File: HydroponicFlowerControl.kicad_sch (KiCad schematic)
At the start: 4 parts

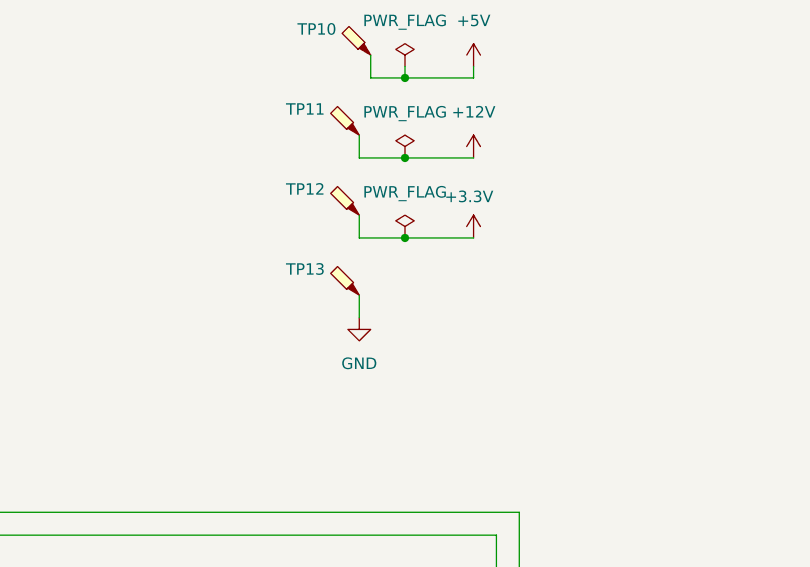
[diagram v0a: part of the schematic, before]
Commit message: Fix ERC warnings
See #28
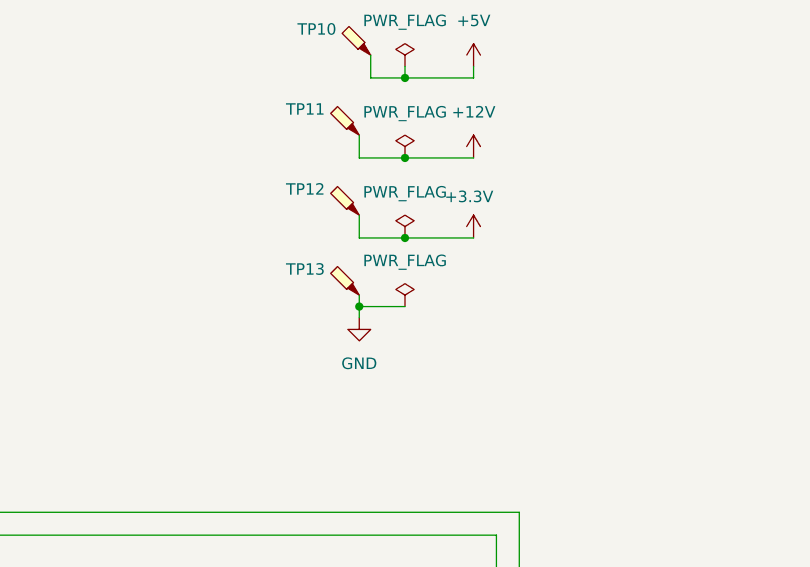
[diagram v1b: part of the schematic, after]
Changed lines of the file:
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@@
+	)
+	(junction
+		(at 104.14 49.53)
+		(diameter 0)
+		(color 0 0 0 0)
 	)
 	(junction
@@
 	(wire
 		(pts
+			(xy 104.14 49.53) (xy 104.14 50.8)
+		)
+		(stroke
+			(width 0)
+			(type default)
+		)
+	)
+	(wire
+		(pts
 			(xy 104.14 39.37) (xy 104.14 41.91)
 		)
@@
 	(wire
 		(pts
-			(xy 104.14 48.26) (xy 104.14 50.8)
+			(xy 104.14 48.26) (xy 104.14 49.53)
 		)
 		(stroke
@@
 		(pts
 			(xy 104.14 33.02) (xy 109.22 33.02)
+		)
+		(stroke
+			(width 0)
+			(type default)
+		)
+	)
+	(wire
+		(pts
+			(xy 104.14 49.53) (xy 109.22 49.53)
 		)
 		(stroke
@@
 	(symbol
 		(lib_id "power:PWR_FLAG")
+		(at 109.22 49.53 0)
+		(unit 1)
+		(exclude_from_sim no)
+		(in_bom yes)
+		(on_board yes)
+		(dnp no)
+		(fields_autoplaced yes)
+		(property "Reference" "#FLG04"
+			(at 109.22 47.625 0)
+			(effects
+				(font
+					(size 1.27 1.27)
+				)
+				(hide yes)
+			)
+		)
+		(property "Value" "PWR_FLAG"
+			(at 109.22 44.45 0)
+			(effects
+				(font
+					(size 1.27 1.27)
+				)
+			)
+		)
+		(property "Footprint" ""
+			(at 109.22 49.53 0)
+			(effects
+				(font
+					(size 1.27 1.27)
+				)
+				(hide yes)
+			)
+		)
+		(property "Datasheet" "~"
+			(at 109.22 49.53 0)
+			(effects
+				(font
+					(size 1.27 1.27)
+				)
+				(hide yes)
+			)
+		)
+		(property "Description" "Special symbol for telling ERC where power comes from"
+			(at 109.22 49.53 0)
+			(effects
+				(font
+					(size 1.27 1.27)
+				)
+				(hide yes)
+			)
+		)
+		(pin "1"
+		)
+		(instances
+			(project "HydroponicFlowerControl"
+				(path "/b3c8a28b-9ce1-4002-b8e8-ef8cb73fe031"
+					(reference "#FLG04")
+					(unit 1)
+				)
+			)
+		)
+	)
+	(symbol
+		(lib_name "PWR_FLAG_1")
+		(lib_id "power:PWR_FLAG")
 		(at 109.22 41.91 0)

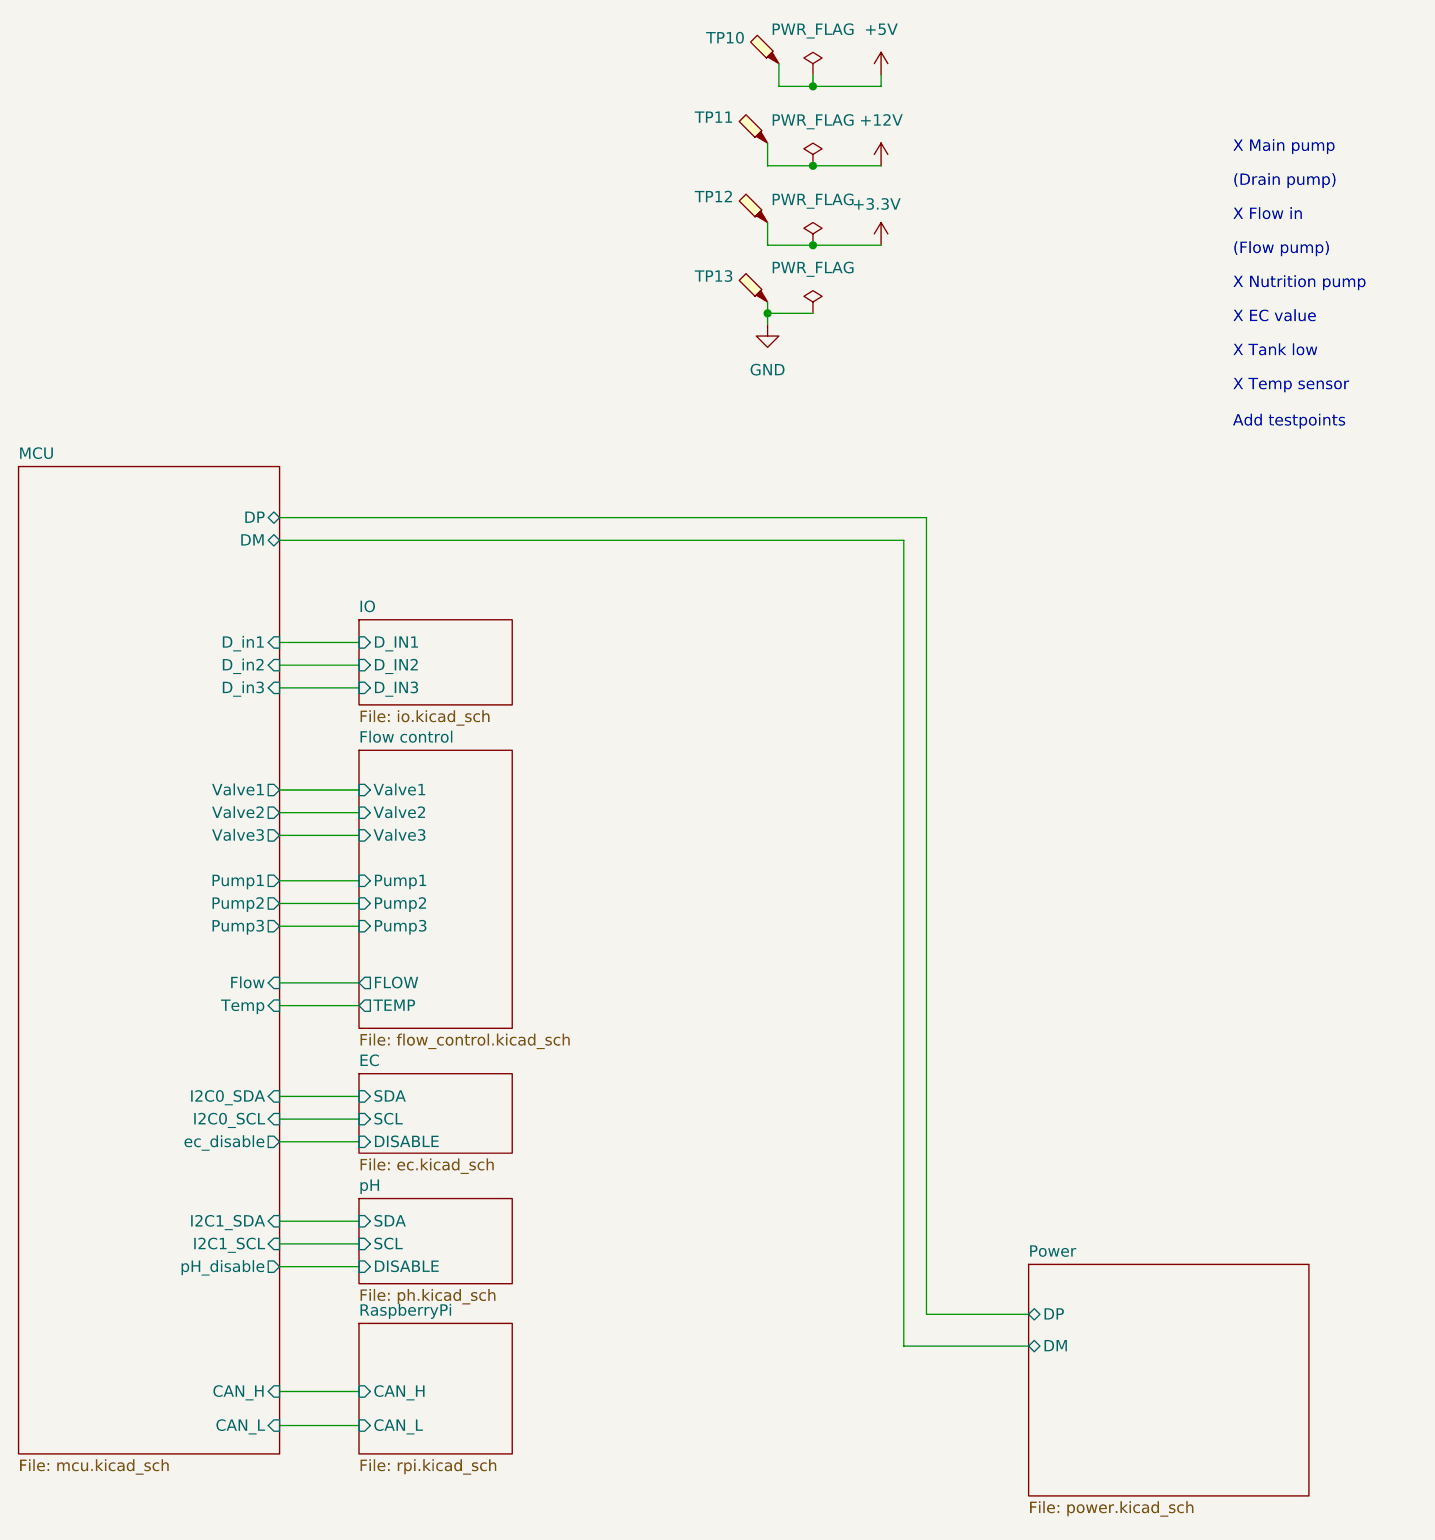
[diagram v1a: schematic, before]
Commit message: Fix ERC errors
Closes #28
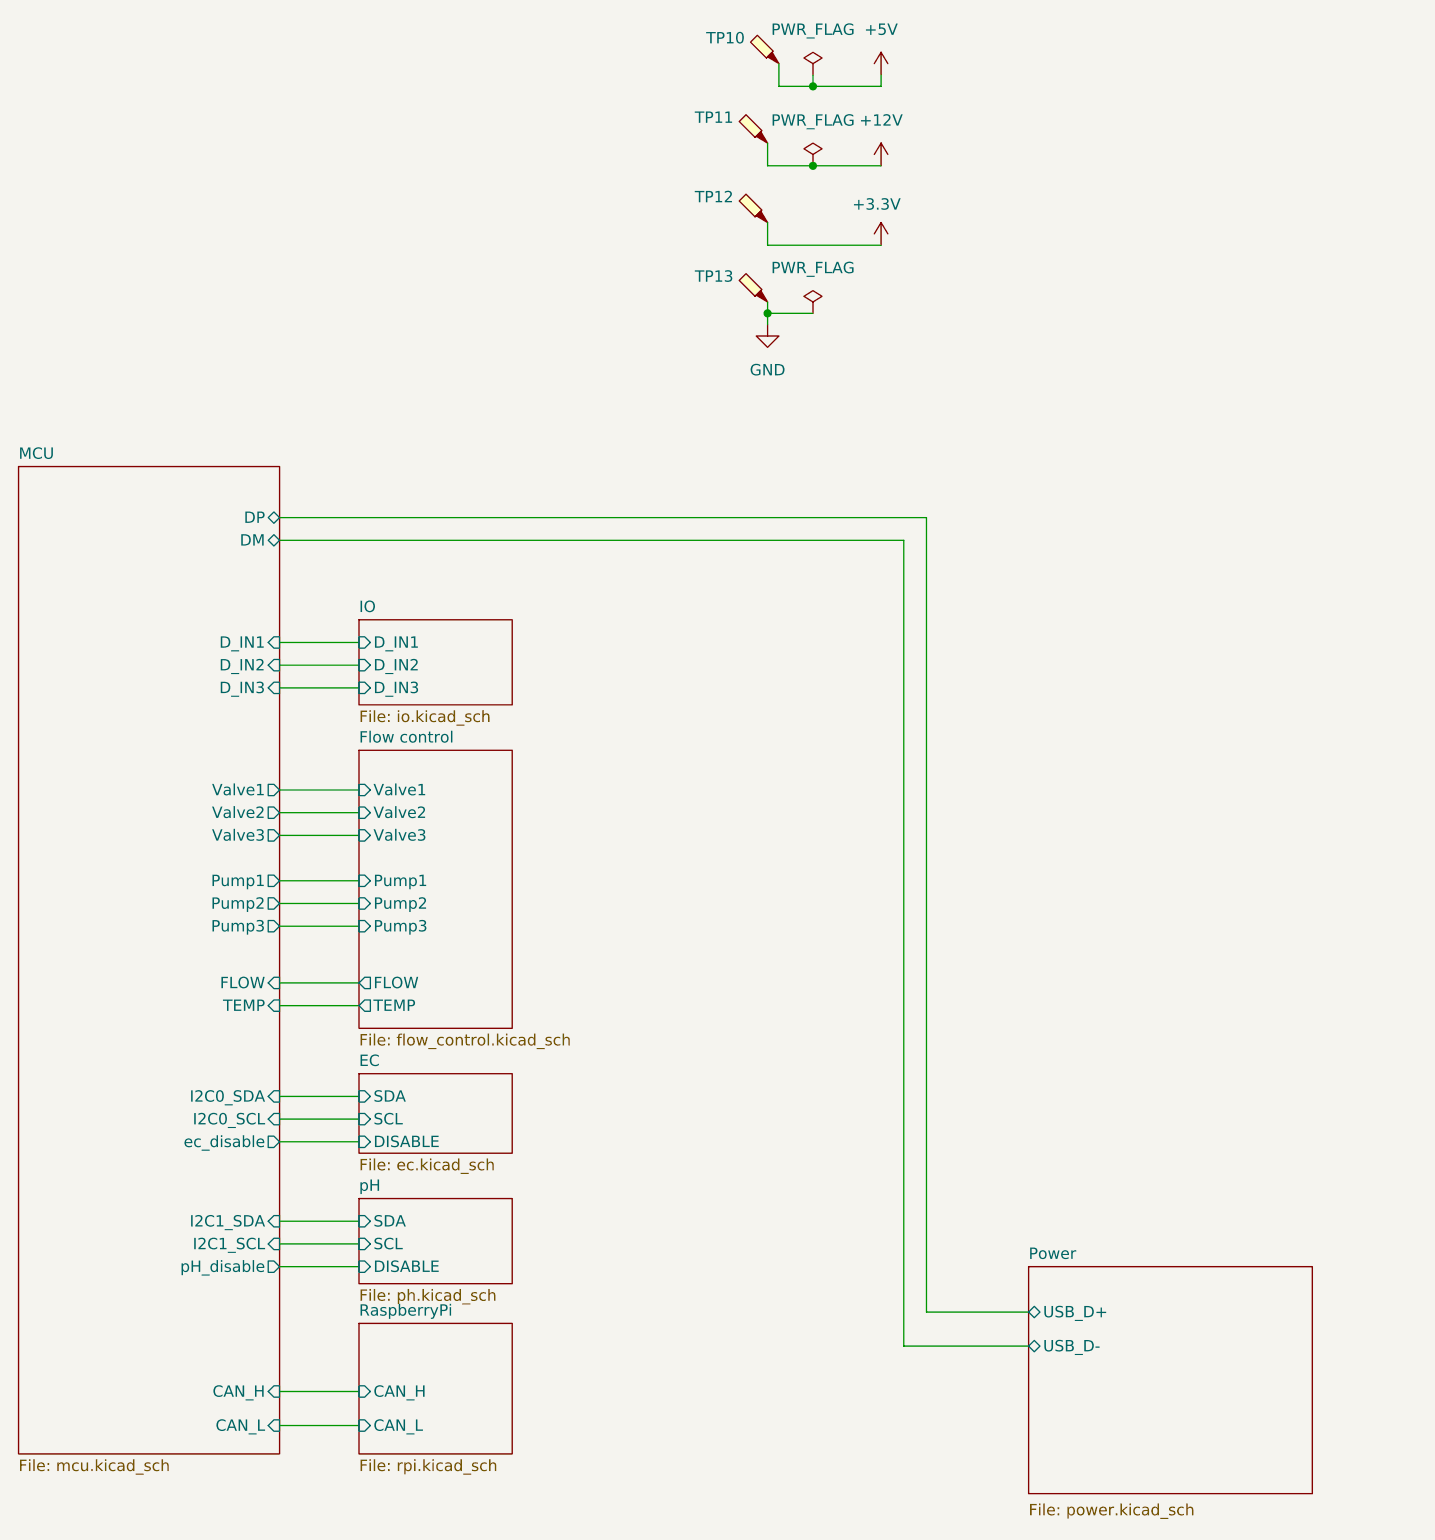
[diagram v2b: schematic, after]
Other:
- sheet MCU ports: added D_IN1, D_IN2, D_IN3, FLOW, TEMP; removed D_in1, D_in2, D_in3, Flow, Temp
- sheet Power ports: added USB_D+, USB_D-; removed DM, DP
- note removed: "(Drain pump)"
- note removed: "(Flow pump)"
- note removed: "Add testpoints"
- note removed: "X EC value"
- note removed: "X Flow in"
- note removed: "X Main pump"
- note removed: "X Nutrition pump"
- note removed: "X Tank low"
- note removed: "X Temp sensor"
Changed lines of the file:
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@@
-	)
-	(junction
-		(at 109.22 41.91)
-		(diameter 0)
-		(color 0 0 0 0)
 	)
 	(junction
@@
 	(wire
 		(pts
-			(xy 121.92 72.39) (xy 121.92 161.544)
+			(xy 121.92 72.39) (xy 121.92 161.29)
 		)
 		(stroke
@@
 	(wire
 		(pts
-			(xy 109.22 41.91) (xy 116.84 41.91)
-		)
-		(stroke
-			(width 0)
-			(type default)
-		)
-	)
-	(wire
-		(pts
 			(xy 49.53 153.67) (xy 58.42 153.67)
 		)
@@
 	(wire
 		(pts
-			(xy 121.92 161.544) (xy 133.35 161.544)
+			(xy 121.92 161.29) (xy 133.35 161.29)
 		)
 		(stroke
@@
 	(wire
 		(pts
-			(xy 104.14 41.91) (xy 109.22 41.91)
+			(xy 104.14 41.91) (xy 116.84 41.91)
 		)
 		(stroke
@@
 			(width 0)
 			(type default)
-		)
-	)
-	(text "X Tank low"
-		(exclude_from_sim no)
-		(at 156.21 54.61 0)
-		(effects
-			(font
-				(size 1.27 1.27)
-			)
-			(justify left bottom)
-		)
-	)
-	(text "X Temp sensor"
-		(exclude_from_sim no)
-		(at 156.21 58.42 0)
-		(effects
-			(font
-				(size 1.27 1.27)
-			)
-			(justify left bottom)
-		)
-	)
-	(text "X EC value"
-		(exclude_from_sim no)
-		(at 156.21 50.8 0)
-		(effects
-			(font
-				(size 1.27 1.27)
-			)
-			(justify left bottom)
-		)
-	)
-	(text "(Drain pump)"
-		(exclude_from_sim no)
-		(at 156.21 35.56 0)
-		(effects
-			(font
-				(size 1.27 1.27)
-			)
-			(justify left bottom)
-		)
-	)
-	(text "(Flow pump)"
-		(exclude_from_sim no)
-		(at 156.21 43.18 0)
-		(effects
-			(font
-				(size 1.27 1.27)
-			)
-			(justify left bottom)
-		)
-	)
-	(text "X Flow in"
-		(exclude_from_sim no)
-		(at 156.21 39.37 0)
-		(effects
-			(font
-				(size 1.27 1.27)
-			)
-			(justify left bottom)
-		)
-	)
-	(text "X Main pump"
-		(exclude_from_sim no)
-		(at 156.21 31.75 0)
-		(effects
-			(font
-				(size 1.27 1.27)
-			)
-			(justify left bottom)
-		)
-	)
-	(text "Add testpoints"
-		(exclude_from_sim no)
-		(at 156.21 62.484 0)
-		(effects
-			(font
-				(size 1.27 1.27)
-			)
-			(justify left bottom)
-		)
-	)
-	(text "X Nutrition pump"
-		(exclude_from_sim no)
-		(at 156.21 46.99 0)
-		(effects
-			(font
-				(size 1.27 1.27)
-			)
-			(justify left bottom)
 		)
 	)
@@
 	)
 	(symbol
-		(lib_name "PWR_FLAG_1")
-		(lib_id "power:PWR_FLAG")
-		(at 109.22 41.91 0)
-		(unit 1)
-		(exclude_from_sim no)
-		(in_bom yes)
-		(on_board yes)
-		(dnp no)
-		(fields_autoplaced yes)
-		(property "Reference" "#FLG03"
-			(at 109.22 40.005 0)
-			(effects
-				(font
-					(size 1.27 1.27)
-				)
-				(hide yes)
-			)
-		)
-		(property "Value" "PWR_FLAG"
-			(at 109.22 36.83 0)
-			(effects
-				(font
-					(size 1.27 1.27)
-				)
-			)
-		)
-		(property "Footprint" ""
-			(at 109.22 41.91 0)
-			(effects
-				(font
-					(size 1.27 1.27)
-				)
-				(hide yes)
-			)
-		)
-		(property "Datasheet" "~"
-			(at 109.22 41.91 0)
-			(effects
-				(font
-					(size 1.27 1.27)
-				)
-				(hide yes)
-			)
-		)
-		(property "Description" "Special symbol for telling ERC where power comes from"
-			(at 109.22 41.91 0)
-			(effects
-				(font
-					(size 1.27 1.27)
-				)
-				(hide yes)
-			)
-		)
-		(pin "1"
-		)
-		(instances
-			(project "HydroponicFlowerControl"
-				(path "/b3c8a28b-9ce1-4002-b8e8-ef8cb73fe031"
-					(reference "#FLG03")
-					(unit 1)
-				)
-			)
-		)
-	)
-	(symbol
 		(lib_id "power:+3.3V")
 		(at 116.84 41.91 0)
@@
 	)
 	(sheet
-		(at 133.35 155.956)
-		(size 31.369 25.908)
+		(at 133.35 156.21)
+		(size 31.75 25.4)
 		(fields_autoplaced yes)
 		(stroke
@@
 		)
 		(property "Sheetname" "Power"
-			(at 133.35 155.2444 0)
+			(at 133.35 155.4984 0)
 			(effects
 				(font
@@
 		)
 		(property "Sheetfile" "power.kicad_sch"
-			(at 133.35 182.4486 0)
+			(at 133.35 182.7026 0)
 			(effects
 				(font
@@
 			)
 		)
-		(pin "DP" bidirectional
-			(at 133.35 161.544 180)
-			(effects
-				(font
-					(size 1.27 1.27)
-				)
-				(justify left)
-			)
-		)
-		(pin "DM" bidirectional
+		(pin "USB_D-" bidirectional
 			(at 133.35 165.1 180)
+			(effects
+				(font
+					(size 1.27 1.27)
+				)
+				(justify left)
+			)
+		)
+		(pin "USB_D+" bidirectional
+			(at 133.35 161.29 180)
 			(effects
 				(font
@@
 			)
 		)
-		(pin "Temp" input
-			(at 49.53 127 0)
-			(effects
-				(font
-					(size 1.27 1.27)
-				)
-				(justify right)
-			)
-		)
-		(pin "Flow" input
-			(at 49.53 124.46 0)
-			(effects
-				(font
-					(size 1.27 1.27)
-				)
-				(justify right)
-			)
-		)
-		(pin "D_in3" input
-			(at 49.53 91.44 0)
-			(effects
-				(font
-					(size 1.27 1.27)
-				)
-				(justify right)
-			)
-		)
-		(pin "D_in1" input
-			(at 49.53 86.36 0)
-			(effects
-				(font
-					(size 1.27 1.27)
-				)
-				(justify right)
-			)
-		)
-		(pin "D_in2" input
-			(at 49.53 88.9 0)
-			(effects
-				(font
-					(size 1.27 1.27)
-				)
-				(justify right)
-			)
-		)
 		(pin "pH_disable" output
 			(at 49.53 156.21 0)
@@
 			(effects
 				(font
+					(size 1.27 1.27)
+				)
+				(justify right)
+			)
+		)
+		(pin "TEMP" input
+			(at 49.53 127 0)
+			(effects
+				(font
+					(size 1.27 1.27)
+				)
+				(justify right)
+			)
+		)
+		(pin "FLOW" input
+			(at 49.53 124.46 0)
+			(effects
+				(font
+					(size 1.27 1.27)
+				)
+				(justify right)
+			)
+		)
+		(pin "D_IN2" input
+			(at 49.53 88.9 0)
+			(effects
+				(font
+					(size 1.27 1.27)
+				)
+				(justify right)
+			)
+		)
+		(pin "D_IN3" input
+			(at 49.53 91.44 0)
+			(effects
+				(font
+					(size 1.27 1.27)
+				)
+				(justify right)
+			)
+		)
+		(pin "D_IN1" input
+			(at 49.53 86.36 0)
+			(effects
+				(font

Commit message: Add 1-Wire
Closes #29
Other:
- sheet IO ports: added 1WIRE; removed none
- sheet RaspberryPi ports: added 1WIRE; removed none
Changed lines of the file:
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@@
+	(wire
+		(pts
+			(xy 86.36 88.9) (xy 86.36 167.64)
+		)
+		(stroke
+			(width 0)
+			(type default)
+		)
+	)
 	(wire
 		(pts
@@
 		(pts
 			(xy 104.14 30.48) (xy 104.14 33.02)
+		)
+		(stroke
+			(width 0)
+			(type default)
+		)
+	)
+	(wire
+		(pts
+			(xy 76.2 88.9) (xy 86.36 88.9)
+		)
+		(stroke
+			(width 0)
+			(type default)
+		)
+	)
+	(wire
+		(pts
+			(xy 76.2 167.64) (xy 86.36 167.64)
 		)
 		(stroke
@@
 	(sheet
 		(at 58.42 162.56)
-		(size 17.145 14.605)
+		(size 17.78 15.24)
 		(fields_autoplaced yes)
 		(stroke
@@
 				)
 				(justify left)
+			)
+		)
+		(pin "1WIRE" bidirectional
+			(at 76.2 167.64 0)
+			(effects
+				(font
+					(size 1.27 1.27)
+				)
+				(justify right)
 			)
 		)
@@
 	(sheet
 		(at 58.42 83.82)
-		(size 17.145 9.525)
+		(size 17.78 10.16)
 		(fields_autoplaced yes)
 		(stroke
@@
 			)
 		)
+		(pin "1WIRE" bidirectional
+			(at 76.2 88.9 0)
+			(effects
+				(font
+					(size 1.27 1.27)
+				)
+				(justify right)
+			)
+		)

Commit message: Add testpoints
Closes #47
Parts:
- added TP17: GND, TestPoint:TestPoint_Pad_D1.5mm, symbol Connector:TestPoint
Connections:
- net GND: now also TP17.1
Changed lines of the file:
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@@
+	)
+	(junction
+		(at 109.22 49.53)
+		(diameter 0)
+		(color 0 0 0 0)
 	)
 	(junction
@@
 		(pts
 			(xy 49.53 72.39) (xy 121.92 72.39)
+		)
+		(stroke
+			(width 0)
+			(type default)
+		)
+	)
+	(wire
+		(pts
+			(xy 109.22 49.53) (xy 115.57 49.53)
 		)
 		(stroke
@@
 					(unit 1)
 				)
+			)
+		)
+	)
+	(symbol
+		(lib_id "Connector:TestPoint")
+		(at 115.57 49.53 0)
+		(unit 1)
+		(exclude_from_sim no)
+		(in_bom no)
+		(on_board yes)
+		(dnp no)
+		(fields_autoplaced yes)
+		(property "Reference" "TP17"
+			(at 118.11 44.9579 0)
+			(effects
+				(font
+					(size 1.27 1.27)
+				)
+				(justify left)
+			)
+		)
+		(property "Value" "GND"
+			(at 118.11 47.4979 0)
+			(effects
+				(font
+					(size 1.27 1.27)
+				)
+				(justify left)
+			)
+		)
+		(property "Footprint" "TestPoint:TestPoint_Pad_D1.5mm"
+			(at 120.65 49.53 0)
+			(effects
+				(font
+					(size 1.27 1.27)
+				)
+				(hide yes)
+			)
+		)
+		(property "Datasheet" "~"
+			(at 120.65 49.53 0)
+			(effects
+				(font
+					(size 1.27 1.27)
+				)
+				(hide yes)
+			)
+		)
+		(property "Description" "test point"
+			(at 115.57 49.53 0)
+			(effects
+				(font
+					(size 1.27 1.27)
+				)
+				(hide yes)
+			)
+		)
+		(pin "1"
+		)
+		(instances
+			(project "HydroponicFlowerControl"
+				(path "/b3c8a28b-9ce1-4002-b8e8-ef8cb73fe031"
+					(reference "TP17")
+					(unit 1)
+				)
